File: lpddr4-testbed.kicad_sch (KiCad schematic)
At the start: 2 parts

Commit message: Update signage
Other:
- moved on the sheet: N1, N2

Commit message: [#45231] globlib
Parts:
- N1: footprint lpddr4-testbed-footprints:antmicro-logo_scaled_20mm -> antmicro-footprints:antmicro-logo; symbol lpddr4-testbed:antmicro_logo -> antmicroMechanicalParts:antmicro_logo
- N2: footprint lpddr4-testbed-footprints:oshw-logo -> antmicro-footprints:oshw-logo; symbol lpddr4-testbed:oshw_logo -> antmicroMechanicalParts:oshw_logo

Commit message: Fix missing global links (wip), designators fixed
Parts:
- N1: footprint antmicro-footprints:antmicro-logo -> antmicro-footprints:antmicro-logo_scaled_20mm
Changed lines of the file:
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@@
       (effects (font (size 1.27 1.27)) (justify left))
     )
-    (property "Footprint" "antmicro-footprints:antmicro-logo" (id 2) (at 107.315 266.7 0)
+    (property "Footprint" "antmicro-footprints:antmicro-logo_scaled_20mm" (id 2) (at 107.315 266.7 0)
       (effects (font (size 1.27 1.27)) hide)
     )
@@
       (reference "C39") (unit 1) (value "C_100n_0402") (footprint "antmicro-footprints:C_0402_1005Metric")
     )
-    (path "/00000000-0000-0000-0000-0000606db5e6/00000000-0000-0000-0000-000060710469"
-      (reference "D1") (unit 1) (value "KP-1608CGCK") (footprint "lpddr4-testbed-footprints:LED_0603")
-    )
-    (path "/00000000-0000-0000-0000-0000606db5e6/00000000-0000-0000-0000-0000607100f6"
-      (reference "D2") (unit 1) (value "KP-1608CGCK") (footprint "lpddr4-testbed-footprints:LED_0603")
-    )
-    (path "/00000000-0000-0000-0000-0000606db5e6/00000000-0000-0000-0000-00006070fbc4"
-      (reference "D3") (unit 1) (value "KP-1608CGCK") (footprint "lpddr4-testbed-footprints:LED_0603")
-    )
-    (path "/00000000-0000-0000-0000-0000606db5e6/00000000-0000-0000-0000-00006070a035"
-      (reference "D4") (unit 1) (value "KP-1608CGCK") (footprint "lpddr4-testbed-footprints:LED_0603")
-    )
-    (path "/00000000-0000-0000-0000-0000606db5e6/00000000-0000-0000-0000-000060df635a"
-      (reference "IC1") (unit 1) (value "PCA6408APW") (footprint "lpddr4-testbed-footprints:TSSOP-16")
-    )
-    (path "/00000000-0000-0000-0000-0000606db5e6/00000000-0000-0000-0000-0000606e74fc"
-      (reference "IC2") (unit 1) (value "AT24CS01") (footprint "lpddr4-testbed-footprints:SOT-23-5")
-    )
-    (path "/00000000-0000-0000-0000-00005fdc4a05/00000000-0000-0000-0000-0000600ac6a9"
-      (reference "J1") (unit 1) (value "ddr4-sodimm-edge-connector") (footprint "lpddr4-testbed-footprints:SODIMM_DDR4_EDGE")
-    )
-    (path "/00000000-0000-0000-0000-00005fdc4a05/00000000-0000-0000-0000-0000600b3548"
-      (reference "J1") (unit 2) (value "ddr4-sodimm-edge-connector") (footprint "lpddr4-testbed-footprints:SODIMM_DDR4_EDGE")
+    (path "/00000000-0000-0000-0000-0000606db5e6/f5c066cb-0b65-4141-b037-5d9434eb10bf"
+      (reference "D1") (unit 1) (value "LED_G_0603_KP-1608CGCK") (footprint "antmicro-footprints:LED_0603_1608Metric_G")
+    )
+    (path "/00000000-0000-0000-0000-0000606db5e6/e8ccee09-815b-4293-857b-4af514aa35d1"
+      (reference "D2") (unit 1) (value "LED_G_0603_KP-1608CGCK") (footprint "antmicro-footprints:LED_0603_1608Metric_G")
+    )
+    (path "/00000000-0000-0000-0000-0000606db5e6/65d78578-4037-46e9-a5d5-c7e84b95e870"
+      (reference "D3") (unit 1) (value "LED_G_0603_KP-1608CGCK") (footprint "antmicro-footprints:LED_0603_1608Metric_G")
+    )
+    (path "/00000000-0000-0000-0000-0000606db5e6/b4823387-7999-4d9a-82f5-027239277691"
+      (reference "D4") (unit 1) (value "LED_G_0603_KP-1608CGCK") (footprint "antmicro-footprints:LED_0603_1608Metric_G")
+    )
+    (path "/00000000-0000-0000-0000-0000606db5e6/a6d712cf-0d3a-438f-839b-c73baf84a038"
+      (reference "IC1") (unit 1) (value "PCA6408A_TSSOP") (footprint "antmicro-footprints:TSSOP-16_4.4x5mm_P0.65mm")
+    )
+    (path "/00000000-0000-0000-0000-0000606db5e6/d0c57e51-b57a-4f24-aff5-9b18460245c1"
+      (reference "IC2") (unit 1) (value "AT24CS01_SOT23") (footprint "antmicro-footprints:SOT-23-5")
+    )
+    (path "/00000000-0000-0000-0000-00005fdc4a05/2f028d8c-89f4-4c25-99fe-1d228fb513c4"
+      (reference "J1") (unit 1) (value "Bus_DDR4_Edge_Conn") (footprint "antmicro-footprints:Bus_DDR4_Conn_Edge")
+    )
+    (path "/00000000-0000-0000-0000-00005fdc4a05/ef5e3531-2cb5-4a73-8680-84a758f618d4"
+      (reference "J1") (unit 2) (value "Bus_DDR4_Edge_Conn") (footprint "antmicro-footprints:Bus_DDR4_Conn_Edge")
     )
     (path "/00000000-0000-0000-0000-0000606db5e6/00000000-0000-0000-0000-00006071b1e8"
@@
     )
     (path "/00000000-0000-0000-0000-00005fff4c1f"
-      (reference "N1") (unit 1) (value "antmicro_logo") (footprint "antmicro-footprints:antmicro-logo")
+      (reference "N1") (unit 1) (value "antmicro_logo") (footprint "antmicro-footprints:antmicro-logo_scaled_20mm")
     )
     (path "/00000000-0000-0000-0000-00005fff48fb"
@@
       (reference "R14") (unit 1) (value "R_10k_0402") (footprint "antmicro-footprints:R_0402_1005Metric")
     )
-    (path "/00000000-0000-0000-0000-0000606db5e6/00000000-0000-0000-0000-000060767927"
-      (reference "TP1") (unit 1) (value "TP_SMD1MM") (footprint "lpddr4-testbed-footprints:Testpoint_smd_1mm")
-    )
-    (path "/00000000-0000-0000-0000-0000606db5e6/00000000-0000-0000-0000-000060765b95"
-      (reference "TP2") (unit 1) (value "TP_SMD1MM") (footprint "lpddr4-testbed-footprints:Testpoint_smd_1mm")
-    )
-    (path "/00000000-0000-0000-0000-0000606db5e6/00000000-0000-0000-0000-0000607450bc"
-      (reference "TP3") (unit 1) (value "TP_SMD1MM") (footprint "lpddr4-testbed-footprints:Testpoint_smd_1mm")
+    (path "/00000000-0000-0000-0000-0000606db5e6/6b30b341-d3b9-4e3a-b9bf-0775b70b2ce7"
+      (reference "TP1") (unit 1) (value "TP_0.75mm_SMD") (footprint "antmicro-footprints:TP_SMD_0.75mm")
+    )
+    (path "/00000000-0000-0000-0000-0000606db5e6/f281abb1-6693-43f4-accc-853b4fbd9492"
+      (reference "TP2") (unit 1) (value "TP_0.75mm_SMD") (footprint "antmicro-footprints:TP_SMD_0.75mm")
+    )
+    (path "/00000000-0000-0000-0000-0000606db5e6/24f5c09f-f562-4b0e-a5b8-a42ca9183bcc"
+      (reference "TP3") (unit 1) (value "TP_0.75mm_SMD") (footprint "antmicro-footprints:TP_SMD_0.75mm")
     )
     (path "/00000000-0000-0000-0000-00005ff943ac/00000000-0000-0000-0000-000060819f73"

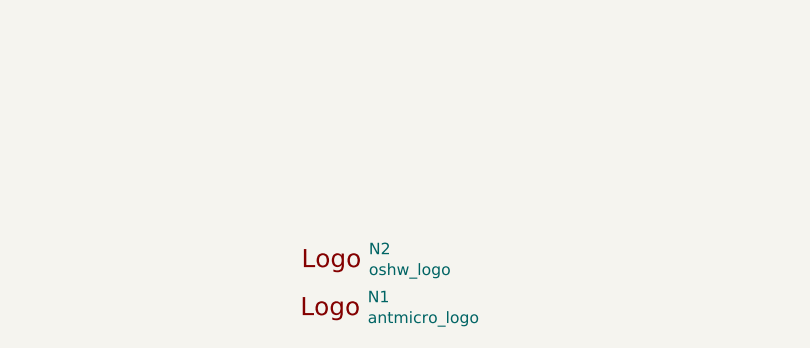
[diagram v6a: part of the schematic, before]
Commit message: Introduce component standardization
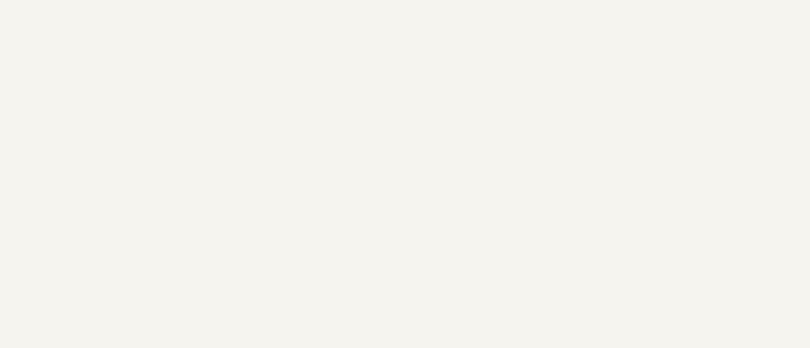
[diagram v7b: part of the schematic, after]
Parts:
- removed N1: antmicro_logo, antmicro-footprints:antmicro-logo_scaled_20mm, symbol antmicroMechanicalParts:antmicro_logo
- removed N2: oshw_logo, antmicro-footprints:oshw-logo, symbol antmicroMechanicalParts:oshw_logo

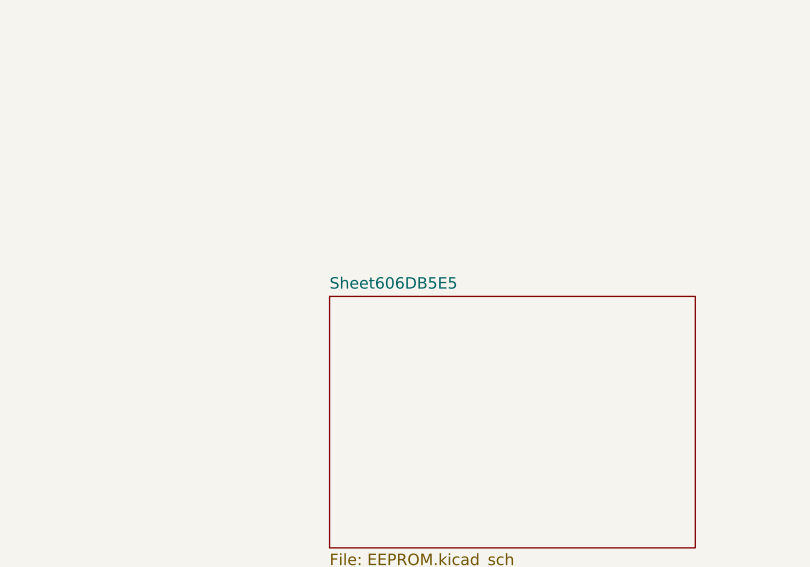
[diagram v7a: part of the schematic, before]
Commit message: [#56947] Correct component references
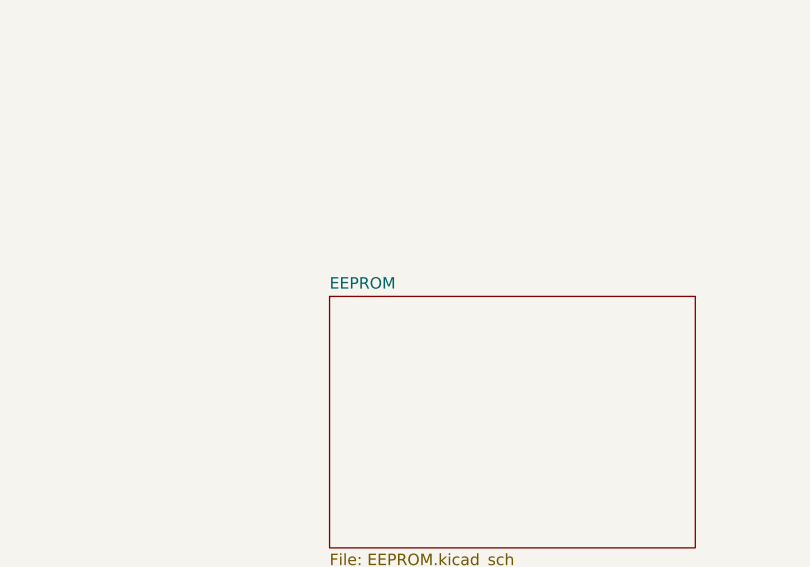
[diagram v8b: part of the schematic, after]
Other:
- sheet Sheet606DB5E5 renamed EEPROM
